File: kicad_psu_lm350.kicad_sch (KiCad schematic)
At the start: 28 parts, among them J1 AC Input, J2 AC Input, J3 DC +1.25 to +30V, J4 GND, J5 GND, J6 GND, J7 GND, U1 LM350_TO220

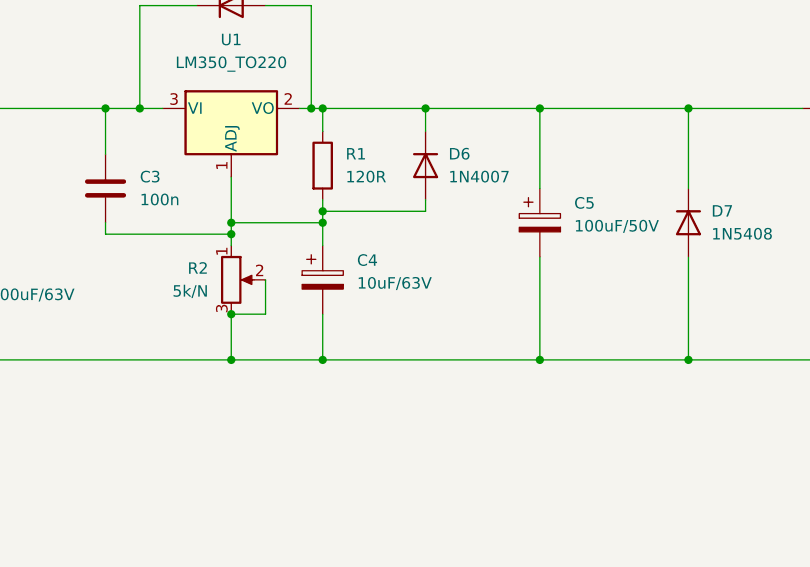
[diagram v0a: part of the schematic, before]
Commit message: Early footprint assignment
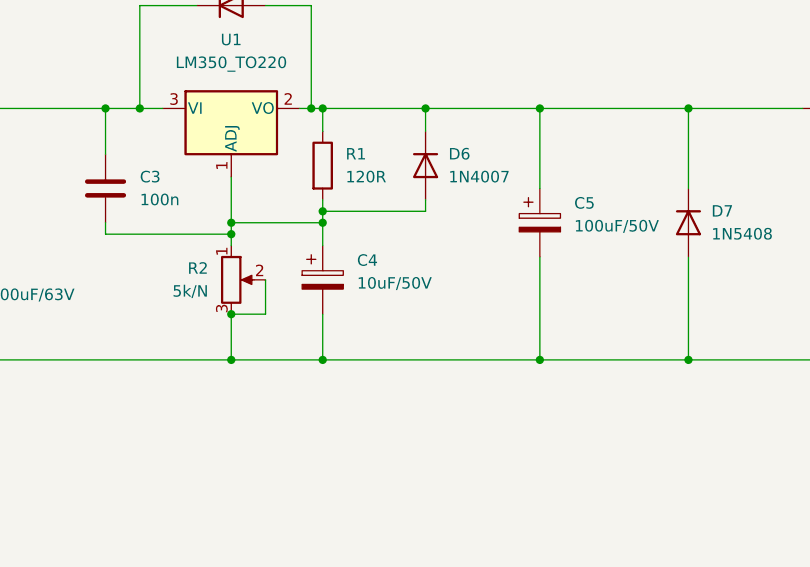
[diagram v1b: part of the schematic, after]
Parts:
- C1, C2: footprint (none) -> Capacitor_THT:CP_Radial_D18.0mm_P7.50mm
- C11, C12, C13, C14, C3: footprint (none) -> Capacitor_THT:C_Disc_D8.0mm_W5.0mm_P5.00mm
- C4: value 10uF/63V -> 10uF/50V; footprint (none) -> Capacitor_THT:CP_Radial_D5.0mm_P2.50mm
- C5: footprint (none) -> Capacitor_THT:CP_Radial_D8.0mm_P3.50mm
- F1, F2: footprint (none) -> Fuse:Fuseholder_Cylinder-5x20mm_Schurter_0031_8201_Horizontal_Open
- R1: footprint (none) -> Resistor_THT:R_Axial_DIN0207_L6.3mm_D2.5mm_P10.16mm_Horizontal
- R2: footprint (none) -> Potentiometer_THT:Potentiometer_Vishay_148-149_Single_Horizontal
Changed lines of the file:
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@@
       (effects (font (size 1.27 1.27)) (justify left))
     )
-    (property "Footprint" "" (id 2) (at 67.0052 63.5 0)
+    (property "Footprint" "Capacitor_THT:C_Disc_D8.0mm_W5.0mm_P5.00mm" (id 2) (at 67.0052 63.5 0)
       (effects (font (size 1.27 1.27)) hide)
     )
@@
       (effects (font (size 1.27 1.27)) (justify left))
     )
-    (property "Footprint" "" (id 2) (at 91.1352 46.99 0)
+    (property "Footprint" "Capacitor_THT:CP_Radial_D18.0mm_P7.50mm" (id 2) (at 91.1352 46.99 0)
       (effects (font (size 1.27 1.27)) hide)
     )
@@
       (effects (font (size 1.27 1.27)) (justify left))
     )
-    (property "Footprint" "" (id 2) (at 44.1452 43.18 0)
+    (property "Footprint" "Capacitor_THT:C_Disc_D8.0mm_W5.0mm_P5.00mm" (id 2) (at 44.1452 43.18 0)
       (effects (font (size 1.27 1.27)) hide)
     )
@@
       (effects (font (size 1.27 1.27)) (justify left))
     )
-    (property "Footprint" "" (id 2) (at 44.1452 63.5 0)
+    (property "Footprint" "Capacitor_THT:C_Disc_D8.0mm_W5.0mm_P5.00mm" (id 2) (at 44.1452 63.5 0)
       (effects (font (size 1.27 1.27)) hide)
     )
@@
     (property "Reference" "F1" (id 0) (at 36.83 39.37 90))
     (property "Value" "3A" (id 1) (at 36.83 41.91 90))
-    (property "Footprint" "" (id 2) (at 36.83 47.498 90)
+    (property "Footprint" "Fuse:Fuseholder_Cylinder-5x20mm_Schurter_0031_8201_Horizontal_Open" (id 2) (at 36.83 47.498 90)
       (effects (font (size 1.27 1.27)) hide)
     )
@@
       (effects (font (size 1.27 1.27)) (justify right))
     )
-    (property "Footprint" "" (id 2) (at 140.97 54.61 0)
+    (property "Footprint" "Potentiometer_THT:Potentiometer_Vishay_148-149_Single_Horizontal" (id 2) (at 140.97 54.61 0)
       (effects (font (size 1.27 1.27)) hide)
     )
@@
     (property "Reference" "F2" (id 0) (at 208.28 29.21 90))
     (property "Value" "3A" (id 1) (at 208.28 31.75 90))
-    (property "Footprint" "" (id 2) (at 208.28 37.338 90)
+    (property "Footprint" "Fuse:Fuseholder_Cylinder-5x20mm_Schurter_0031_8201_Horizontal_Open" (id 2) (at 208.28 37.338 90)
       (effects (font (size 1.27 1.27)) hide)
     )
@@
       (effects (font (size 1.27 1.27)) (justify left))
     )
-    (property "Footprint" "" (id 2) (at 176.2252 52.07 0)
+    (property "Footprint" "Capacitor_THT:CP_Radial_D8.0mm_P3.50mm" (id 2) (at 176.2252 52.07 0)
       (effects (font (size 1.27 1.27)) hide)
     )
@@
       (effects (font (size 1.27 1.27)) (justify left))
     )
-    (property "Footprint" "" (id 2) (at 67.0052 43.18 0)
+    (property "Footprint" "Capacitor_THT:C_Disc_D8.0mm_W5.0mm_P5.00mm" (id 2) (at 67.0052 43.18 0)
       (effects (font (size 1.27 1.27)) hide)
     )
@@
       (effects (font (size 1.27 1.27)) (justify left))
     )
-    (property "Footprint" "" (id 2) (at 149.352 41.91 90)
+    (property "Footprint" "Resistor_THT:R_Axial_DIN0207_L6.3mm_D2.5mm_P10.16mm_Horizontal" (id 2) (at 149.352 41.91 90)
       (effects (font (size 1.27 1.27)) hide)
     )
@@
       (effects (font (size 1.27 1.27)) (justify left))
     )
-    (property "Value" "10uF/63V" (id 1) (at 154.94 54.9909 0)
-      (effects (font (size 1.27 1.27)) (justify left))
-    )
-    (property "Footprint" "" (id 2) (at 152.0952 58.42 0)
+    (property "Value" "10uF/50V" (id 1) (at 154.94 54.9909 0)
+      (effects (font (size 1.27 1.27)) (justify left))
+    )
+    (property "Footprint" "Capacitor_THT:CP_Radial_D5.0mm_P2.50mm" (id 2) (at 152.0952 58.42 0)
       (effects (font (size 1.27 1.27)) hide)
     )
@@
       (effects (font (size 1.27 1.27)) (justify left))
     )
-    (property "Footprint" "" (id 2) (at 110.1852 59.69 0)
+    (property "Footprint" "Capacitor_THT:CP_Radial_D18.0mm_P7.50mm" (id 2) (at 110.1852 59.69 0)
       (effects (font (size 1.27 1.27)) hide)
     )
@@
       (effects (font (size 1.27 1.27)) (justify left))
     )
-    (property "Footprint" "" (id 2) (at 127.9652 48.26 0)
+    (property "Footprint" "Capacitor_THT:C_Disc_D8.0mm_W5.0mm_P5.00mm" (id 2) (at 127.9652 48.26 0)
       (effects (font (size 1.27 1.27)) hide)
     )
@@
   (symbol_instances
     (path "/16ebe0e1-7c2d-4dcd-92c1-d5795c393526"
-      (reference "C1") (unit 1) (value "2200uF/63V") (footprint "")
+      (reference "C1") (unit 1) (value "2200uF/63V") (footprint "Capacitor_THT:CP_Radial_D18.0mm_P7.50mm")
     )
     (path "/df9d6c83-fb20-44c1-a195-378ec0ac70a8"
-      (reference "C2") (unit 1) (value "2200uF/63V") (footprint "")
+      (reference "C2") (unit 1) (value "2200uF/63V") (footprint "Capacitor_THT:CP_Radial_D18.0mm_P7.50mm")
     )
     (path "/fe73ecfe-37d8-4a7d-9893-8be04410b96e"
-      (reference "C3") (unit 1) (value "100n") (footprint "")
+      (reference "C3") (unit 1) (value "100n") (footprint "Capacitor_THT:C_Disc_D8.0mm_W5.0mm_P5.00mm")
     )
     (path "/d10252b4-c827-45ed-8521-3abfc1cbf8bd"
-      (reference "C4") (unit 1) (value "10uF/63V") (footprint "")
+      (reference "C4") (unit 1) (value "10uF/50V") (footprint "Capacitor_THT:CP_Radial_D5.0mm_P2.50mm")
     )
     (path "/9419fb54-f666-48b4-a21c-d94dc134ad22"
-      (reference "C5") (unit 1) (value "100uF/50V") (footprint "")
+      (reference "C5") (unit 1) (value "100uF/50V") (footprint "Capacitor_THT:CP_Radial_D8.0mm_P3.50mm")
     )
     (path "/4de1a620-4ed6-44ea-a81b-02c5d78ff5bc"
-      (reference "C11") (unit 1) (value "100n") (footprint "")
+      (reference "C11") (unit 1) (value "100n") (footprint "Capacitor_THT:C_Disc_D8.0mm_W5.0mm_P5.00mm")
     )
     (path "/9c883022-2b8c-4314-a90b-6b5a23d97e26"
-      (reference "C12") (unit 1) (value "100n") (footprint "")
+      (reference "C12") (unit 1) (value "100n") (footprint "Capacitor_THT:C_Disc_D8.0mm_W5.0mm_P5.00mm")
     )
     (path "/6bdc6027-c717-42c0-8300-7269e5a4a250"
-      (reference "C13") (unit 1) (value "100n") (footprint "")
+      (reference "C13") (unit 1) (value "100n") (footprint "Capacitor_THT:C_Disc_D8.0mm_W5.0mm_P5.00mm")
     )
     (path "/15fc7d4b-77c3-45c6-bbd6-00d38bd0c703"
-      (reference "C14") (unit 1) (value "100n") (footprint "")
+      (reference "C14") (unit 1) (value "100n") (footprint "Capacitor_THT:C_Disc_D8.0mm_W5.0mm_P5.00mm")
     )
     (path "/1e34201d-ee26-4d15-adc0-c42dae394575"
@@
     )
     (path "/74fd94e2-473e-4f46-9c06-7eb1a161c57f"
-      (reference "F1") (unit 1) (value "3A") (footprint "")
+      (reference "F1") (unit 1) (value "3A") (footprint "Fuse:Fuseholder_Cylinder-5x20mm_Schurter_0031_8201_Horizontal_Open")
     )
     (path "/85ca7656-4110-4600-8bd1-ea5e4c686182"
-      (reference "F2") (unit 1) (value "3A") (footprint "")
+      (reference "F2") (unit 1) (value "3A") (footprint "Fuse:Fuseholder_Cylinder-5x20mm_Schurter_0031_8201_Horizontal_Open")
     )
     (path "/c5b4af5a-4182-4f7b-8b77-09d41637d816"
@@
     )
     (path "/d096da25-6227-4be6-97a1-e3403179ce78"
-      (reference "R1") (unit 1) (value "120R") (footprint "")
+      (reference "R1") (unit 1) (value "120R") (footprint "Resistor_THT:R_Axial_DIN0207_L6.3mm_D2.5mm_P10.16mm_Horizontal")
     )
     (path "/82b0dec0-162c-4e44-b3c3-ac4e561cc8c8"
-      (reference "R2") (unit 1) (value "5k/N") (footprint "")
+      (reference "R2") (unit 1) (value "5k/N") (footprint "Potentiometer_THT:Potentiometer_Vishay_148-149_Single_Horizontal")
     )
     (path "/d43ce4c8-6022-4d25-a1c7-1f2fb257e071"

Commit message: Early PCB placement
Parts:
- J1, J2, J3, J4, J5, J6, J7: footprint (none) -> Connector_PinSocket_2.54mm:PinSocket_1x01_P2.54mm_Vertical
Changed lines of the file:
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@@
     (title "PSU 3A with LM350")
     (date "2022-12-29")
-    (rev "0.1")
+    (rev "0.2")
     (company "Henryk Paluch")
   )
@@
   (junction (at 140.97 58.42) (diameter 0) (color 0 0 0 0)
   )
+  (junction (at 43.18 35.56) (diameter 0) (color 0 0 0 0)
+  )
   (junction (at 151.13 63.5) (diameter 0) (color 0 0 0 0)
   )
@@
     (stroke (width 0) (type default) (color 0 0 0 0))
   )
+  (wire (pts (xy 43.18 31.75) (xy 43.18 35.56))
+    (stroke (width 0) (type default) (color 0 0 0 0))
+  )
   (wire (pts (xy 217.17 86.36) (xy 217.17 78.74))
     (stroke (width 0) (type default) (color 0 0 0 0))
@@
   (wire (pts (xy 144.78 54.61) (xy 144.78 58.42))
     (stroke (width 0) (type default) (color 0 0 0 0))
+  )
+  (symbol (lib_id "power:PWR_FLAG") (at 43.18 31.75 0) (unit 1)
+    (in_bom yes) (on_board yes)
+    (property "Reference" "#FLG01" (id 0) (at 43.18 27.94 0))
+    (property "Value" "PWR_FLAG" (id 1) (at 43.18 25.4 0))
+    (property "Footprint" "" (id 2) (at 43.18 31.75 0)
+      (effects (font (size 1.27 1.27)) hide)
+    )
+    (property "Datasheet" "~" (id 3) (at 43.18 31.75 0)
+      (effects (font (size 1.27 1.27)) hide)
+    )
+    (pin "1")
   )
   (symbol (lib_id "Device:C") (at 66.04 59.69 0) (unit 1)
@@
     (property "Reference" "J2" (id 0) (at 27.305 48.26 0))
     (property "Value" "AC Input" (id 1) (at 27.305 50.8 0))
-    (property "Footprint" "" (id 2) (at 26.67 53.34 0)
+    (property "Footprint" "Connector_PinSocket_2.54mm:PinSocket_1x01_P2.54mm_Vertical" (id 2) (at 26.67 53.34 0)
       (effects (font (size 1.27 1.27)) hide)
     )
@@
     (property "Reference" "J5" (id 0) (at 226.695 66.04 0))
     (property "Value" "GND" (id 1) (at 226.695 68.58 0))
-    (property "Footprint" "" (id 2) (at 227.33 71.12 0)
+    (property "Footprint" "Connector_PinSocket_2.54mm:PinSocket_1x01_P2.54mm_Vertical" (id 2) (at 227.33 71.12 0)
       (effects (font (size 1.27 1.27)) hide)
     )
@@
     (property "Reference" "J3" (id 0) (at 224.155 30.48 0))
     (property "Value" "DC +1.25 to +30V" (id 1) (at 224.155 33.02 0))
-    (property "Footprint" "" (id 2) (at 224.79 35.56 0)
+    (property "Footprint" "Connector_PinSocket_2.54mm:PinSocket_1x01_P2.54mm_Vertical" (id 2) (at 224.79 35.56 0)
       (effects (font (size 1.27 1.27)) hide)
     )
@@
     (property "Reference" "J4" (id 0) (at 226.695 58.42 0))
     (property "Value" "GND" (id 1) (at 226.695 60.96 0))
-    (property "Footprint" "" (id 2) (at 227.33 63.5 0)
+    (property "Footprint" "Connector_PinSocket_2.54mm:PinSocket_1x01_P2.54mm_Vertical" (id 2) (at 227.33 63.5 0)
       (effects (font (size 1.27 1.27)) hide)
     )
@@
     (property "Reference" "J1" (id 0) (at 27.305 40.64 0))
     (property "Value" "AC Input" (id 1) (at 27.305 43.18 0))
-    (property "Footprint" "" (id 2) (at 26.67 45.72 0)
+    (property "Footprint" "Connector_PinSocket_2.54mm:PinSocket_1x01_P2.54mm_Vertical" (id 2) (at 26.67 45.72 0)
       (effects (font (size 1.27 1.27)) hide)
     )
@@
     (property "Reference" "J7" (id 0) (at 226.695 81.28 0))
     (property "Value" "GND" (id 1) (at 226.695 83.82 0))
-    (property "Footprint" "" (id 2) (at 227.33 86.36 0)
+    (property "Footprint" "Connector_PinSocket_2.54mm:PinSocket_1x01_P2.54mm_Vertical" (id 2) (at 227.33 86.36 0)
       (effects (font (size 1.27 1.27)) hide)
     )
@@
     (property "Reference" "J6" (id 0) (at 226.695 73.66 0))
     (property "Value" "GND" (id 1) (at 226.695 76.2 0))
-    (property "Footprint" "" (id 2) (at 227.33 78.74 0)
+    (property "Footprint" "Connector_PinSocket_2.54mm:PinSocket_1x01_P2.54mm_Vertical" (id 2) (at 227.33 78.74 0)
       (effects (font (size 1.27 1.27)) hide)
     )
@@
   )
   (symbol_instances
+    (path "/0947c729-8853-4143-add8-5f6ef355aa2c"
+      (reference "#FLG01") (unit 1) (value "PWR_FLAG") (footprint "")
+    )
     (path "/16ebe0e1-7c2d-4dcd-92c1-d5795c393526"
       (reference "C1") (unit 1) (value "2200uF/63V") (footprint "Capacitor_THT:CP_Radial_D18.0mm_P7.50mm")
@@
     )
     (path "/c5b4af5a-4182-4f7b-8b77-09d41637d816"
-      (reference "J1") (unit 1) (value "AC Input") (footprint "")
+      (reference "J1") (unit 1) (value "AC Input") (footprint "Connector_PinSocket_2.54mm:PinSocket_1x01_P2.54mm_Vertical")
     )
     (path "/2cf30df9-d0cb-455d-8016-81d34bc62ee1"
-      (reference "J2") (unit 1) (value "AC Input") (footprint "")
+      (reference "J2") (unit 1) (value "AC Input") (footprint "Connector_PinSocket_2.54mm:PinSocket_1x01_P2.54mm_Vertical")
     )
     (path "/3d73ff94-8e97-4909-97b1-6aabb5e5f826"
-      (reference "J3") (unit 1) (value "DC +1.25 to +30V") (footprint "")
+      (reference "J3") (unit 1) (value "DC +1.25 to +30V") (footprint "Connector_PinSocket_2.54mm:PinSocket_1x01_P2.54mm_Vertical")
     )
     (path "/beea8495-7452-475c-ab7d-8018210a2074"
-      (reference "J4") (unit 1) (value "GND") (footprint "")
+      (reference "J4") (unit 1) (value "GND") (footprint "Connector_PinSocket_2.54mm:PinSocket_1x01_P2.54mm_Vertical")
     )
     (path "/37c2b0e6-7c43-4c16-bb76-7e3d93041930"
-      (reference "J5") (unit 1) (value "GND") (footprint "")
+      (reference "J5") (unit 1) (value "GND") (footprint "Connector_PinSocket_2.54mm:PinSocket_1x01_P2.54mm_Vertical")
     )
     (path "/f0d3b04b-ae34-40d0-a5a2-ddef5a1cdcda"
-      (reference "J6") (unit 1) (value "GND") (footprint "")
+      (reference "J6") (unit 1) (value "GND") (footprint "Connector_PinSocket_2.54mm:PinSocket_1x01_P2.54mm_Vertical")
     )
     (path "/e0868477-e49e-4ac7-a701-36a2c6eba916"
-      (reference "J7") (unit 1) (value "GND") (footprint "")
+      (reference "J7") (unit 1) (value "GND") (footprint "Connector_PinSocket_2.54mm:PinSocket_1x01_P2.54mm_Vertical")
     )
     (path "/d096da25-6227-4be6-97a1-e3403179ce78"

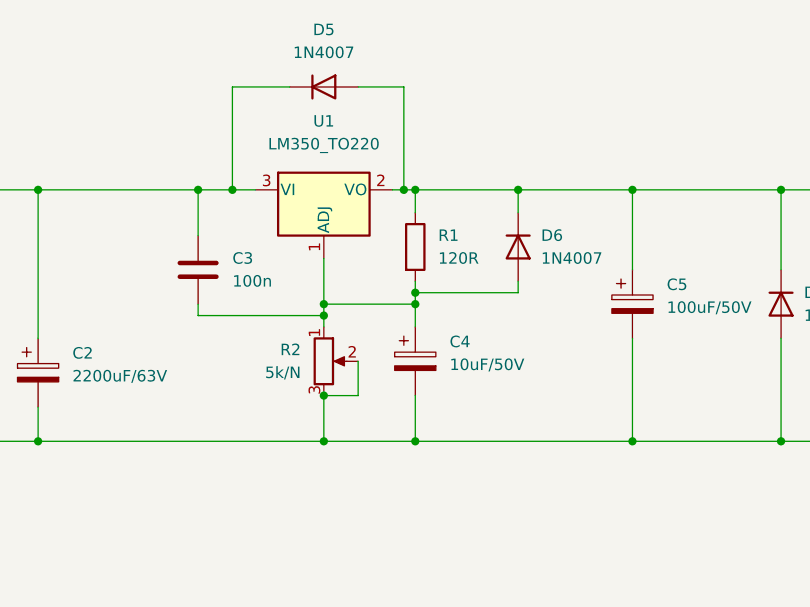
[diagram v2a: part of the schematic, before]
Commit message: Swapped pot pins, aligned schematic nets
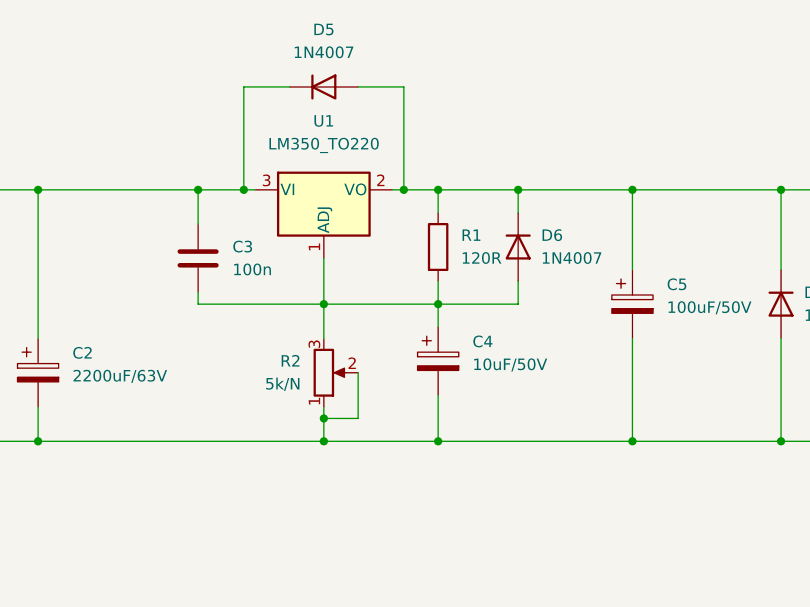
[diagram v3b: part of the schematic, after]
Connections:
- net at C1.2, C13.2, C14.2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: now also R2.1; no longer R2.3
- net at C3.2, C4.1, D6.2 (A)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: now also R2.3; no longer R2.1
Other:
- moved on the sheet: C3, C4, R1, R2

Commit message: C4 should be tantalum to filter HF noise
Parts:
- C4: value 10uF/50V -> 1uF/50V; Cap Type (none) -> tantalum
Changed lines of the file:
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@@
   (title_block
     (title "PSU 3A with LM350")
-    (date "2022-12-29")
-    (rev "0.3")
+    (date "2022-12-30")
+    (rev "0.40")
     (company "Henryk Paluch")
   )
@@
   )
   (symbol (lib_id "Device:C_Polarized") (at 153.67 54.61 0) (unit 1)
-    (in_bom yes) (on_board yes) (fields_autoplaced)
+    (in_bom yes) (on_board yes)
     (property "Reference" "C4" (id 0) (at 157.48 52.4509 0)
       (effects (font (size 1.27 1.27)) (justify left))
     )
-    (property "Value" "10uF/50V" (id 1) (at 157.48 54.9909 0)
+    (property "Value" "1uF/50V" (id 1) (at 157.48 54.9909 0)
       (effects (font (size 1.27 1.27)) (justify left))
     )
@@
     (property "Datasheet" "~" (id 3) (at 153.67 54.61 0)
       (effects (font (size 1.27 1.27)) hide)
+    )
+    (property "Cap Type" "tantalum" (id 4) (at 161.29 57.15 0)
+      (effects (font (size 1.27 1.27) italic))
     )
     (pin "1")
@@
     )
     (path "/d10252b4-c827-45ed-8521-3abfc1cbf8bd"
-      (reference "C4") (unit 1) (value "10uF/50V") (footprint "Capacitor_THT:CP_Radial_D5.0mm_P2.50mm")
+      (reference "C4") (unit 1) (value "1uF/50V") (footprint "Capacitor_THT:CP_Radial_D5.0mm_P2.50mm")
     )
     (path "/9419fb54-f666-48b4-a21c-d94dc134ad22"
